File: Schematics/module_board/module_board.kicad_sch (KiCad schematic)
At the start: 30 parts, among them J1 Conn_01x01_Male, J10 Conn_01x01_Male, J2 Conn_01x01_Male, J3 Conn_01x01_Male, J4 Conn_01x01_Male, J5 Conn_01x01_Male, J6 Conn_01x01_Male, J7 Conn_01x01_Male, J8 Conn_01x01_Male, J9 Conn_01x01_Male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

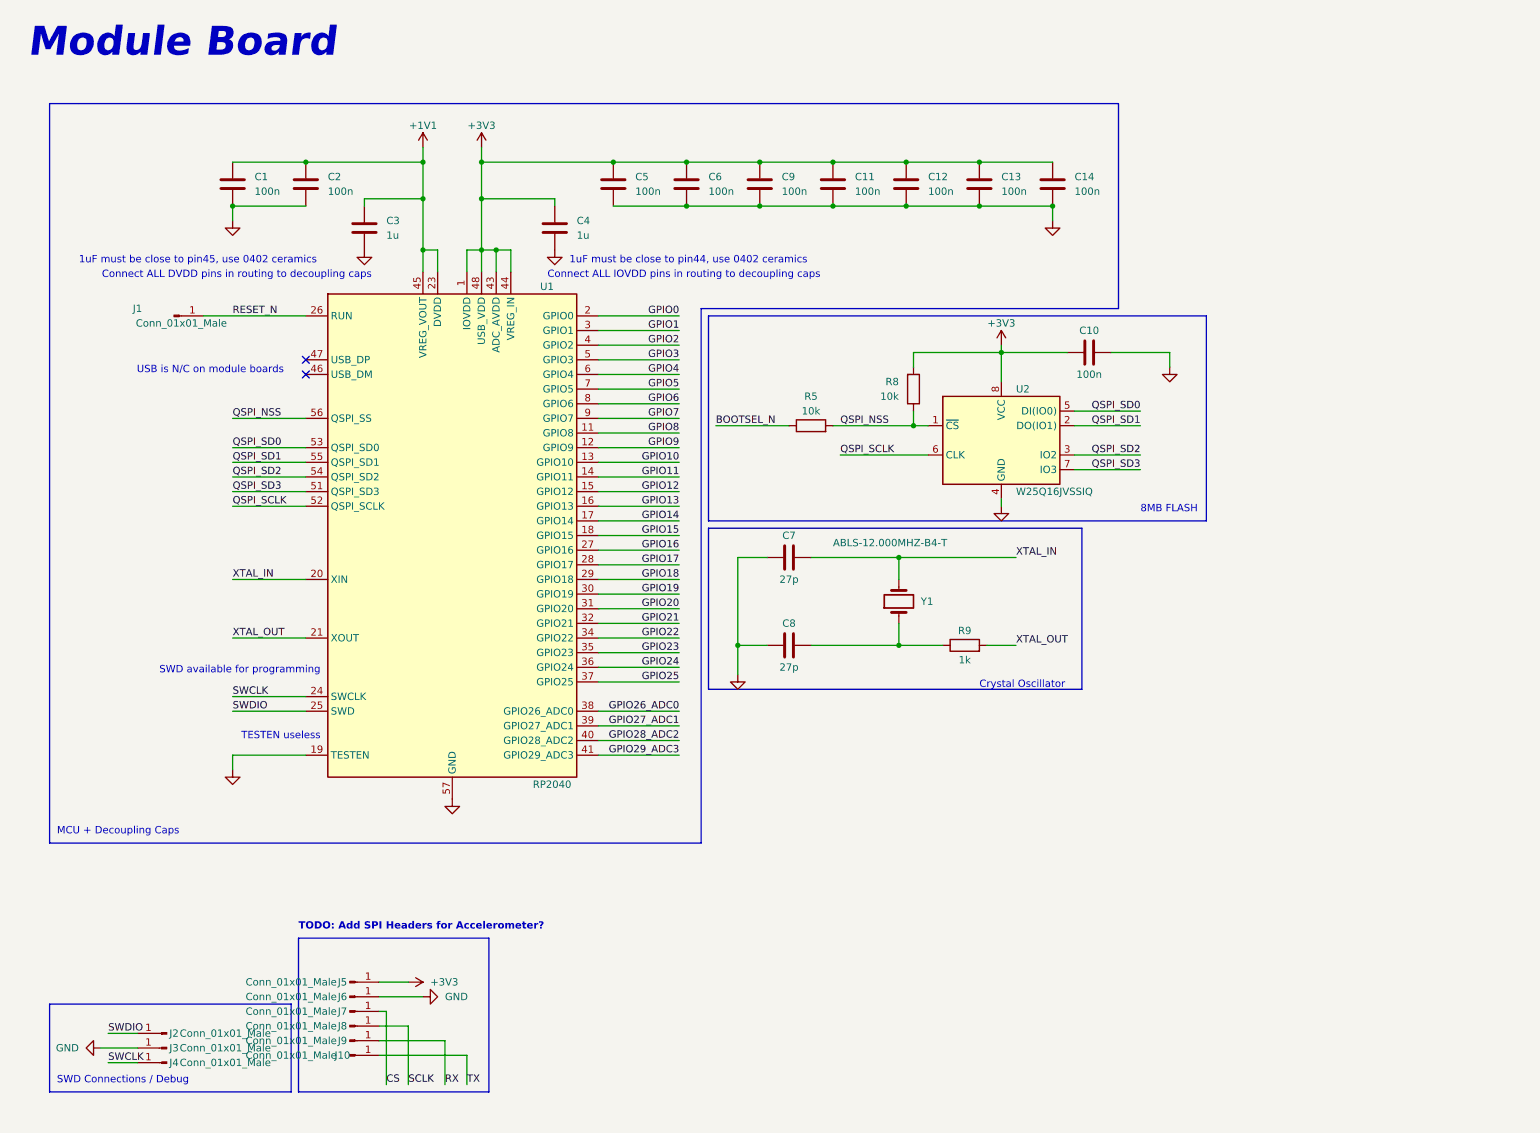
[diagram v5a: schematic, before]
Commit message: Updated Schematic Nets, added Jumper
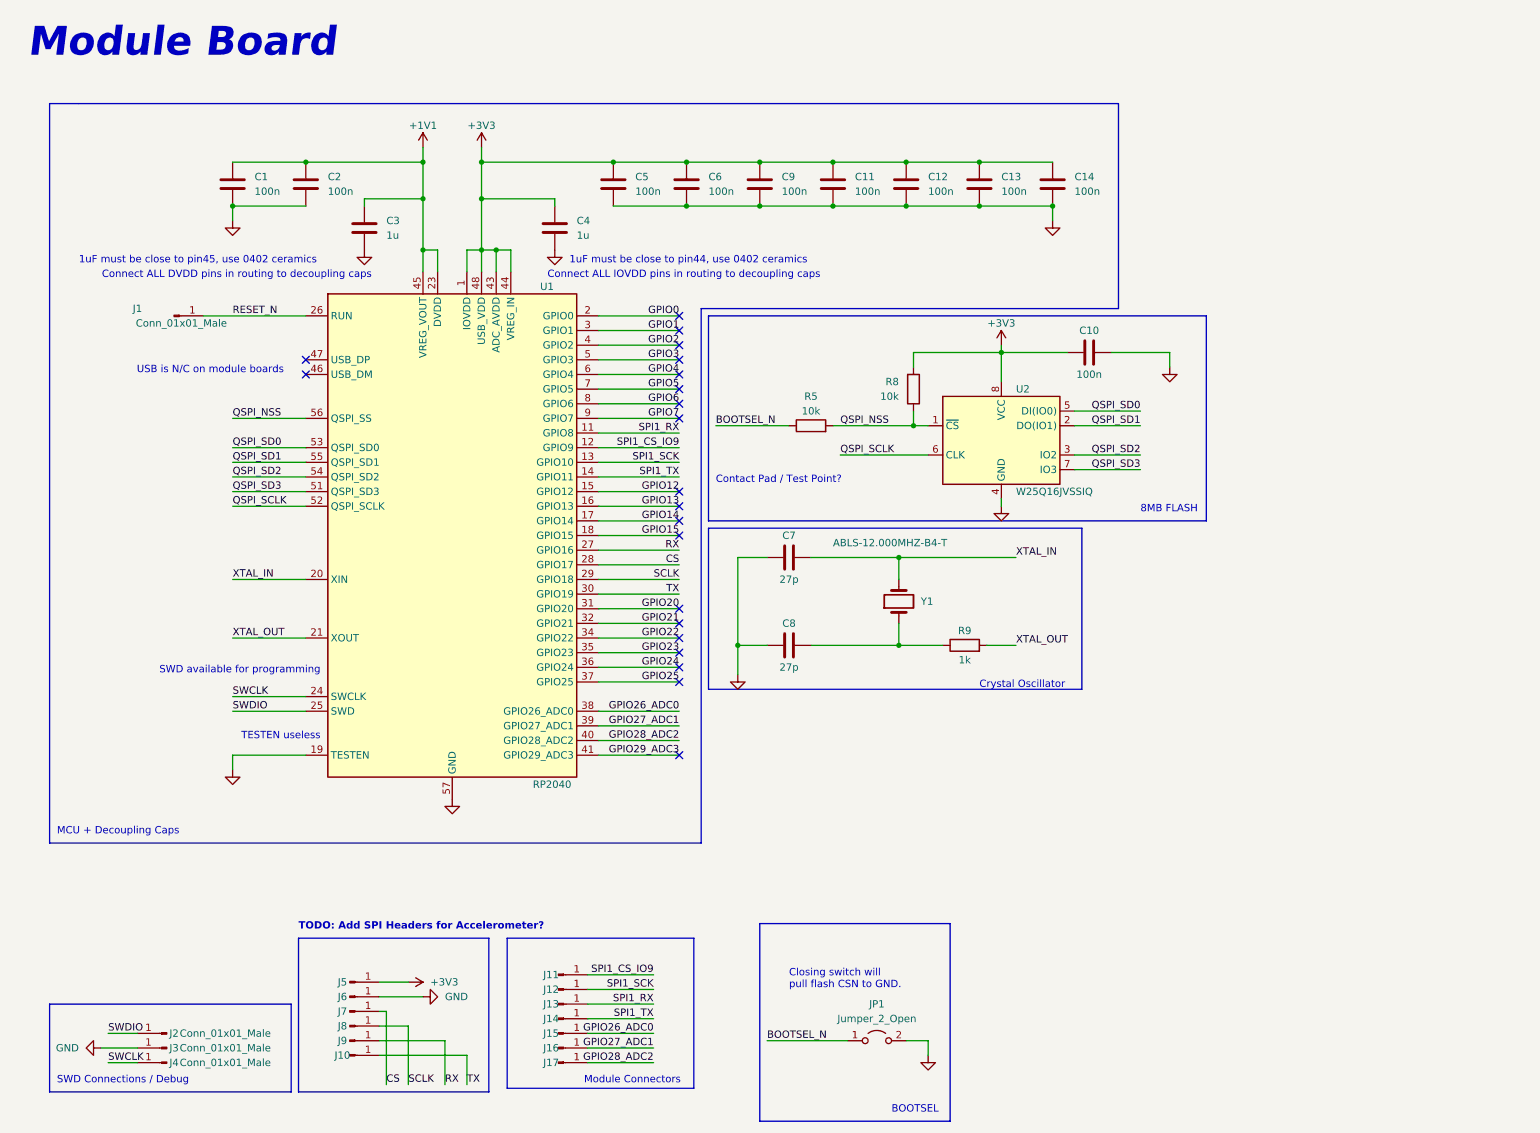
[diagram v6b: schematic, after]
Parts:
- added J11, J12, J13, J14, J15, J16, J17: Conn_01x01_Male, TestPoint:TestPoint_Plated_Hole_D2.0mm, symbol Connector:Conn_01x01_Male
- added JP1: Jumper_2_Open, Jumper:SolderJumper-2_P1.3mm_Open_Pad1.0x1.5mm, symbol Jumper:Jumper_2_Open
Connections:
- net GPIO16 is gone; now on net RX: U1.27 (GPIO16)
- net GPIO17 is gone; now on net CS: U1.28 (GPIO17)
- net GPIO18 is gone; now on net SCLK: U1.29 (GPIO18)
- net GPIO19 is gone; now on net TX: U1.30 (GPIO19)
- net BOOTSEL_N: now also JP1.1 (A)
- net GND: now also JP1.2 (B)
- net GPIO26_ADC0: now also J15.1 (Pin_1)
- net GPIO27_ADC1: now also J16.1 (Pin_1)
- net GPIO28_ADC2: now also J17.1 (Pin_1)
- net GPIO10 renamed SPI1_SCK
- net SPI1_SCK: now also J12.1 (Pin_1)
- net GPIO11 renamed SPI1_TX
- net SPI1_TX: now also J14.1 (Pin_1)
- net GPIO8 renamed SPI1_RX
- net SPI1_RX: now also J13.1 (Pin_1)
- net GPIO9 renamed SPI1_CS_IO9
- net SPI1_CS_IO9: now also J11.1 (Pin_1)
- no-connect marks 2 -> 21
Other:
- note added: "BOOTSEL"
- note added: "Closing switch will pull flash CSN to GND."
- note added: "Contact Pad / Test Point?"
- note added: "Module Connectors"

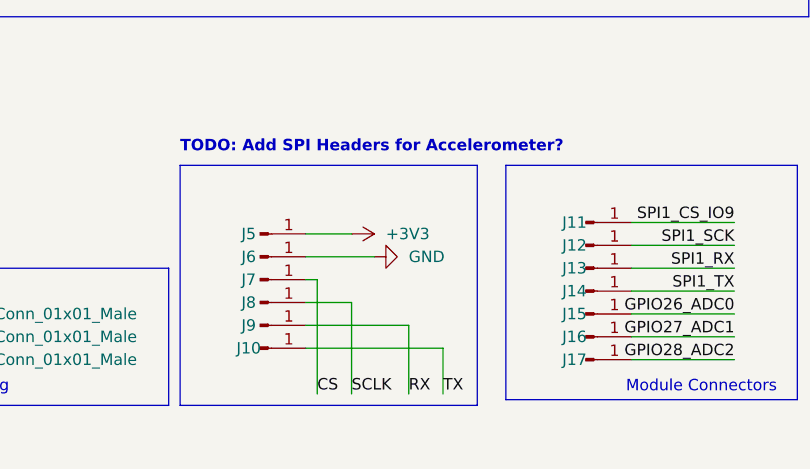
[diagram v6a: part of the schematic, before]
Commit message: Completed PCB Routing, Reassigned Pins, Assigned Pogo Footprint
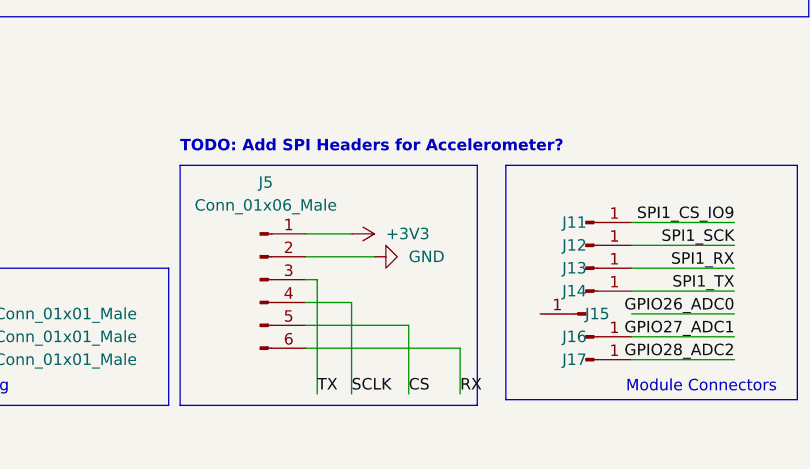
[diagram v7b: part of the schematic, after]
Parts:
- removed J10, J5, J6, J7, J8, J9: Conn_01x01_Male, TestPoint:TestPoint_Plated_Hole_D2.0mm, symbol Connector:Conn_01x01_Male
- added J5: Conn_01x06_Male, Prototroller:Mag_Pogo_6P_P2.2mm_Male, symbol Connector:Conn_01x06_Male
- J1, J2, J3, J4: footprint TestPoint:TestPoint_Pad_D2.0mm -> TestPoint:TestPoint_Pad_D1.0mm
- J11, J12, J13, J14, J15, J16, J17: footprint TestPoint:TestPoint_Plated_Hole_D2.0mm -> Connector_Pin:Pin_D1.0mm_L10.0mm
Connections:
- net +3V3: now also J5.1 (Pin_1)
- net CS: now also J5.5 (Pin_5)
- net GND: now also J5.2 (Pin_2)
- net GPIO26_ADC0: no longer J15.1 (Pin_1)
- net RX: now also J5.6 (Pin_6)
- net SCLK: now also J5.4 (Pin_4)
- net TX: now also J5.3 (Pin_3)
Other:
- moved on the sheet: J15
